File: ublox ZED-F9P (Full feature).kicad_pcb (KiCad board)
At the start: 4 copper layers, 90 x 50 mm, 93 parts, among them J2 CONN_06NO_SILK_FEMALE_PTH, J4 Molex_PicoBlade, J6 CONN_06NO_SILK_FEMALE_PTH, J7 JST_GH, P1 USB_C_Plug_USB2.0, P2 USB_C_Plug_USB2.0, U1 LD1117S33TR, U3 ZED-F9P, U4 ZED-F9H

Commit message: added logo;
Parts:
- added ?: , Qwiic GPS-RTK-SMA - ublox ZED-F9P:LOGO_HGR_1cm, B.Cu at (164.6, 96.2)
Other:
- board text added: "power"
- board text removed: "Power"

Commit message: finished export
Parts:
- moved ? 32.5 mm to (197.0, 95.9)
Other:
- board text added: "ZED-F9x GNSS Module V1.0"
- board text removed: "GNSS Module"
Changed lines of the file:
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@@
   (page A4)
   (title_block
-    (title "GNSS module (with moving base)")
+    (title "ZED-F9x GNSS module (with moving base)")
     (date 2020-09-24)
-    (rev V2)
+    (rev V1)
     (company HiveGround)
     (comment 1 "Jirayu Sirivorawong")
@@
       (psa4output false)
       (plotreference true)
-      (plotvalue true)
+      (plotvalue false)
       (plotinvisibletext false)
       (padsonsilk false)
-      (subtractmaskfromsilk false)
+      (subtractmaskfromsilk true)
       (outputformat 1)
       (mirror false)
-      (drillshape 1)
+      (drillshape 0)
       (scaleselection 1)
-      (outputdirectory ""))
+      (outputdirectory "output/"))
   )
   (net 0 "")
@@
   )
   (module "Qwiic GPS-RTK-SMA - ublox ZED-F9P:LOGO_HGR_1cm" (layer B.Cu)
-    (at 164.592 96.2025 180)
+    (at 197.0405 95.885 180)
     (fp_text reference "" (at -0.0635 -6.477) (layer F.SilkS) hide
       (effects (font (size 1.524 1.524) (thickness 0.3)))
@@
     (effects (font (size 0.5 0.5) (thickness 0.125)))
   )
-  (gr_text "GNSS Module" (at 194.025 97.3) (layer F.SilkS)
-    (effects (font (size 1.5 1.5) (thickness 0.3)))
+  (gr_text "ZED-F9x GNSS Module V1.0" (at 163.6395 97.409) (layer F.SilkS)
+    (effects (font (size 0.762 0.762) (thickness 0.1905)))
   )
   (gr_text "PWR LED" (at 202.675 61.225) (layer B.SilkS)

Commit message: finished v1.1
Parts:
- R5: footprint Resistor_SMD:R_0603_1608Metric_Pad1.05x0.95mm_HandSolder -> Qwiic GPS-RTK-SMA - ublox ZED-F9P:0603
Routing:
- net Net-(D12-Pad2): track 12.3 -> 22.8 mm
- net Net-(D1-Pad2): track 8.05 -> 0.00 mm
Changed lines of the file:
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@@
     (add_net "Net-(U4-Pad6)")
   )
+  (module "Qwiic GPS-RTK-SMA - ublox ZED-F9P:0603" (layer F.Cu)
+    (at 132.2872 92.5165 180)
+    (descr "<p><b>Generic 1608 (0603) package</b></p>\n<p>0.2mm courtyard excess rounded to nearest 0.05mm.</p>")
+    (fp_text reference R5 (at 0 -0.762) (layer F.SilkS)
+      (effects (font (size 0.57912 0.57912) (thickness 0.115824)) (justify bottom))
+    )
+    (fp_text value 1k (at -2.032 -0.254) (layer F.Fab)
+      (effects (font (size 0.57912 0.57912) (thickness 0.115824)) (justify top))
+    )
+    (fp_poly (pts (xy -0.1999 0.3) (xy 0.1999 0.3) (xy 0.1999 -0.3) (xy -0.1999 -0.3)) (layer F.Adhes) (width 0))
+    (fp_poly (pts (xy 0.3302 0.4699) (xy 0.8303 0.4699) (xy 0.8303 -0.4801) (xy 0.3302 -0.4801)) (layer F.Fab) (width 0))
+    (fp_poly (pts (xy -0.8382 0.4699) (xy -0.3381 0.4699) (xy -0.3381 -0.4801) (xy -0.8382 -0.4801)) (layer F.Fab) (width 0))
+    (fp_line (start -0.356 0.419) (end 0.356 0.419) (layer F.Fab) (width 0.1016))
+    (fp_line (start -0.356 -0.432) (end 0.356 -0.432) (layer F.Fab) (width 0.1016))
+    (fp_line (start -1.6 0.7) (end -1.6 -0.7) (layer Dwgs.User) (width 0.0508))
+    (fp_line (start 1.6 0.7) (end -1.6 0.7) (layer Dwgs.User) (width 0.0508))
+    (fp_line (start 1.6 -0.7) (end 1.6 0.7) (layer Dwgs.User) (width 0.0508))
+    (fp_line (start -1.6 -0.7) (end 1.6 -0.7) (layer Dwgs.User) (width 0.0508))
+    (pad 2 smd rect (at 0.85 0 180) (size 1.1 1) (layers F.Cu F.Paste F.Mask)
+      (net 5 "Net-(D2-PadC)") (solder_mask_margin 0.1016))
+    (pad 1 smd rect (at -0.85 0 180) (size 1.1 1) (layers F.Cu F.Paste F.Mask)
+      (net 1 /BACKUP) (solder_mask_margin 0.1016))
+  )
   (module "Qwiic GPS-RTK-SMA - ublox ZED-F9P:LOGO_HGR_1cm" (layer B.Cu)
     (at 197.0405 95.885 180)
@@
   )
   (module Resistor_SMD:R_0603_1608Metric_Pad1.05x0.95mm_HandSolder (layer F.Cu)
-    (at 132.2872 92.5165 180)
-    (descr "Resistor SMD 0603 (1608 Metric), square (rectangular) end terminal, IPC_7351 nominal with elongated pad for handsoldering. (Body size source: http://www.tortai-tech.com/upload/download/2011102023233369053.pdf), generated with kicad-footprint-generator")
-    (tags "resistor handsolder")
-    (attr smd)
-    (fp_text reference R5 (at 3.1372 0.0165) (layer F.SilkS)
-      (effects (font (size 1 1) (thickness 0.15)))
-    )
-    (fp_text value 1k (at 0 1.43) (layer F.Fab)
-      (effects (font (size 1 1) (thickness 0.15)))
-    )
-    (fp_line (start 1.65 0.73) (end -1.65 0.73) (layer F.CrtYd) (width 0.05))
-    (fp_line (start 1.65 -0.73) (end 1.65 0.73) (layer F.CrtYd) (width 0.05))
-    (fp_line (start -1.65 -0.73) (end 1.65 -0.73) (layer F.CrtYd) (width 0.05))
-    (fp_line (start -1.65 0.73) (end -1.65 -0.73) (layer F.CrtYd) (width 0.05))
-    (fp_line (start -0.171267 0.51) (end 0.171267 0.51) (layer F.SilkS) (width 0.12))
-    (fp_line (start -0.171267 -0.51) (end 0.171267 -0.51) (layer F.SilkS) (width 0.12))
-    (fp_line (start 0.8 0.4) (end -0.8 0.4) (layer F.Fab) (width 0.1))
-    (fp_line (start 0.8 -0.4) (end 0.8 0.4) (layer F.Fab) (width 0.1))
-    (fp_line (start -0.8 -0.4) (end 0.8 -0.4) (layer F.Fab) (width 0.1))
-    (fp_line (start -0.8 0.4) (end -0.8 -0.4) (layer F.Fab) (width 0.1))
-    (fp_text user %R (at 0 0) (layer F.Fab)
-      (effects (font (size 0.4 0.4) (thickness 0.06)))
-    )
-    (pad 2 smd roundrect (at 0.875 0 180) (size 1.05 0.95) (layers F.Cu F.Paste F.Mask) (roundrect_rratio 0.25)
-      (net 5 "Net-(D2-PadC)"))
-    (pad 1 smd roundrect (at -0.875 0 180) (size 1.05 0.95) (layers F.Cu F.Paste F.Mask) (roundrect_rratio 0.25)
-      (net 1 /BACKUP))
-    (model ${KISYS3DMOD}/Resistor_SMD.3dshapes/R_0603_1608Metric.wrl
-      (at (xyz 0 0 0))
-      (scale (xyz 1 1 1))
-      (rotate (xyz 0 0 0))
-    )
-  )
-  (module Resistor_SMD:R_0603_1608Metric_Pad1.05x0.95mm_HandSolder (layer F.Cu)
     (at 152.5 91.5)
     (descr "Resistor SMD 0603 (1608 Metric), square (rectangular) end terminal, IPC_7351 nominal with elongated pad for handsoldering. (Body size source: http://www.tortai-tech.com/upload/download/2011102023233369053.pdf), generated with kicad-footprint-generator")
@@
   (segment (start 198.575 58.175) (end 194.775 61.975) (width 0.508) (layer B.Cu) (net 65))
   (segment (start 192.9 61.975) (end 190.5 61.975) (width 0.508) (layer F.Cu) (net 65))
+  (segment (start 184.6842 55.0668) (end 186.6388 55.0668) (width 0.508) (layer F.Cu) (net 65))
+  (segment (start 190.5 58.928) (end 190.5 61.975) (width 0.508) (layer F.Cu) (net 65))
+  (segment (start 186.6388 55.0668) (end 190.5 58.928) (width 0.508) (layer F.Cu) (net 65))
   (segment (start 205.8002 61.2418) (end 203.8832 61.2418) (width 0.2032) (layer F.Cu) (net 66))
   (segment (start 126.8542 61.6786) (end 124.9372 61.6786) (width 0.2032) (layer F.Cu) (net 67))
@@
   (segment (start 161.786 59.5383) (end 161.786 57.3789) (width 0.2032) (layer F.Cu) (net 98))
   (segment (start 162.9004 60.6527) (end 161.786 59.5383) (width 0.2032) (layer F.Cu) (net 98))
-  (segment (start 184.6842 55.0668) (end 187 57.3826) (width 0.508) (layer F.Cu) (net 99))
-  (segment (start 187.45 57.8326) (end 187 57.3826) (width 0.508) (layer F.Cu) (net 99))
-  (segment (start 187.45 61.975) (end 187.45 57.8326) (width 0.508) (layer F.Cu) (net 99))
   (zone (net 2) (net_name GND) (layer In2.Cu) (hatch edge 0.508)
     (connect_pads (clearance 0.508))

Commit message: genereated output
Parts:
- removed the D1 at (187.4, 63.9)
- renumbered D12 to D1

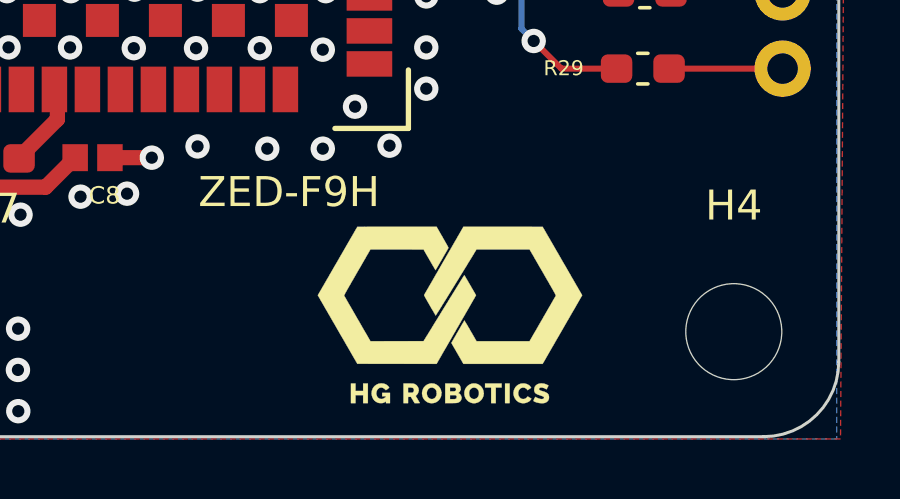
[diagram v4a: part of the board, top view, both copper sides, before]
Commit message: deleted unused files
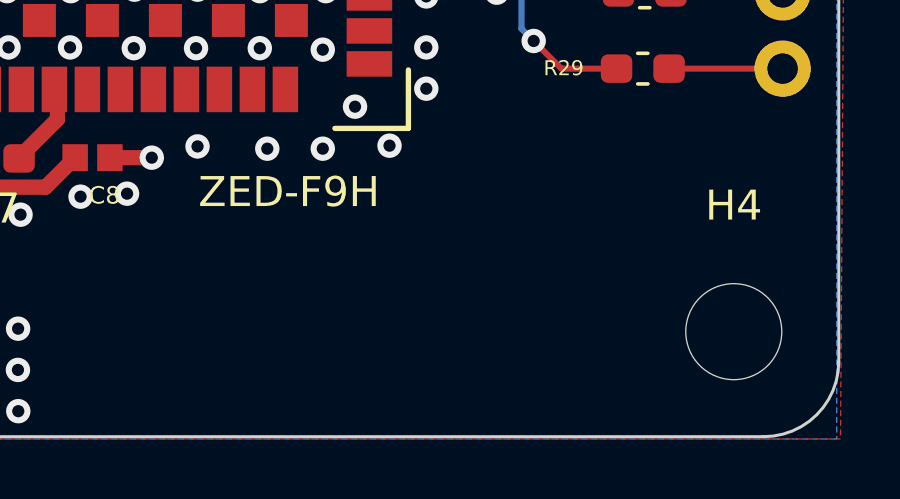
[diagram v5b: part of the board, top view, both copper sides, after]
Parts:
- removed ?: , Qwiic GPS-RTK-SMA - ublox ZED-F9P:LOGO_HGR_1cm
